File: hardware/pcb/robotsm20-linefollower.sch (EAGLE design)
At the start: 139 parts, among them Q5 BSS138LT3G, Q6 BSS138LT3G, Q7 BSS138LT3G, Q8 BSS138LT3G, U1 STM32F405RG

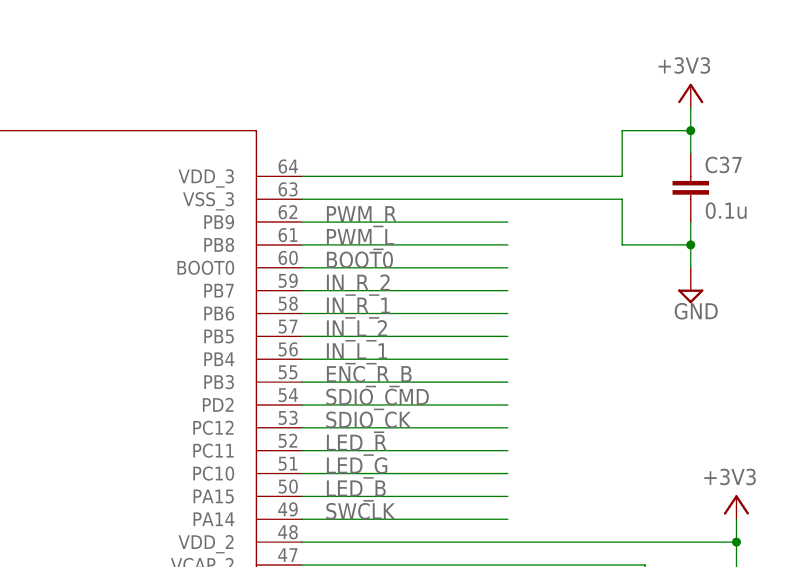
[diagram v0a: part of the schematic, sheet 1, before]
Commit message: Changed pinout on MCU for better layout to motor driver
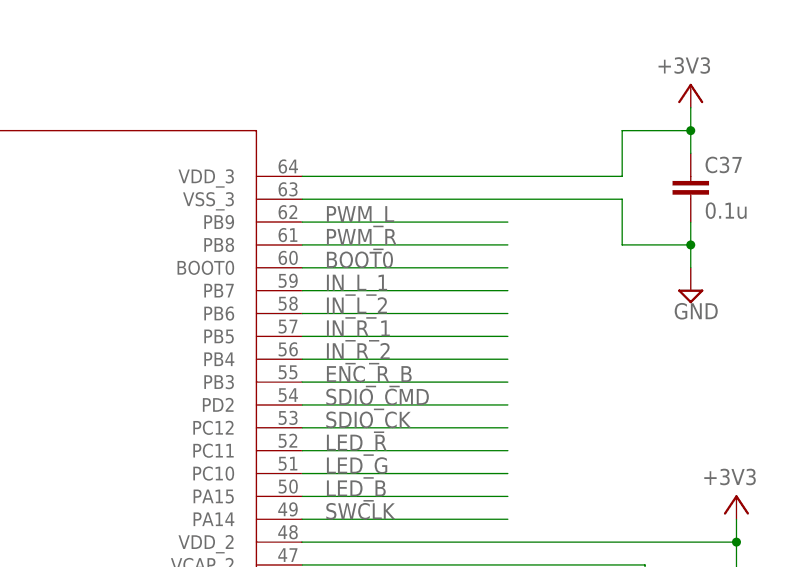
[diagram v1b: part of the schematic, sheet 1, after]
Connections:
- net IN_L_1: now also U1.PB7; no longer U1.PB4
- net IN_L_2: now also U1.PB6; no longer U1.PB5
- net IN_R_1: now also U1.PB5; no longer U1.PB6
- net IN_R_2: now also U1.PB4; no longer U1.PB7
- net PWM_L: now also U1.PB9; no longer U1.PB8
- net PWM_R: now also U1.PB8; no longer U1.PB9
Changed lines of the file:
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@@
 <?xml version="1.0" encoding="utf-8"?>
 <!DOCTYPE eagle SYSTEM "eagle.dtd">
-<eagle version="9.5.2">
+<eagle version="9.6.0">
 <drawing>
 <settings>
@@
 <net name="PWM_L" class="0">
 <segment>
-<wire x1="2.54" y1="15.24" x2="-20.32" y2="15.24" width="0.1524" layer="91"/>
-<pinref part="U1" gate="STM32F405RG" pin="PB8"/>
-<label x="-17.78" y="15.24" size="1.778" layer="95"/>
-</segment>
-</net>
-<net name="PWM_R" class="0">
-<segment>
-<wire x1="2.54" y1="17.78" x2="-20.32" y2="17.78" width="0.1524" layer="91"/>
 <pinref part="U1" gate="STM32F405RG" pin="PB9"/>
+<wire x1="-20.32" y1="17.78" x2="2.54" y2="17.78" width="0.1524" layer="91"/>
 <label x="-17.78" y="17.78" size="1.778" layer="95"/>
-</segment>
-</net>
-<net name="IN_R_2" class="0">
-<segment>
-<wire x1="2.54" y1="10.16" x2="-20.32" y2="10.16" width="0.1524" layer="91"/>
-<pinref part="U1" gate="STM32F405RG" pin="PB7"/>
-<label x="-17.78" y="10.16" size="1.778" layer="95"/>
 </segment>
 </net>
@@
 </segment>
 </net>
-<net name="IN_L_2" class="0">
-<segment>
-<wire x1="2.54" y1="5.08" x2="-20.32" y2="5.08" width="0.1524" layer="91"/>
-<pinref part="U1" gate="STM32F405RG" pin="PB5"/>
-<label x="-17.78" y="5.08" size="1.778" layer="95"/>
-</segment>
-</net>
-<net name="IN_R_1" class="0">
-<segment>
-<wire x1="2.54" y1="7.62" x2="-20.32" y2="7.62" width="0.1524" layer="91"/>
-<pinref part="U1" gate="STM32F405RG" pin="PB6"/>
-<label x="-17.78" y="7.62" size="1.778" layer="95"/>
-</segment>
-</net>
 <net name="ENC_R_B" class="0">
 <segment>
@@
 <pinref part="U1" gate="STM32F405RG" pin="PB3"/>
 <label x="-17.78" y="0" size="1.778" layer="95"/>
-</segment>
-</net>
-<net name="IN_L_1" class="0">
-<segment>
-<wire x1="2.54" y1="2.54" x2="-20.32" y2="2.54" width="0.1524" layer="91"/>
-<pinref part="U1" gate="STM32F405RG" pin="PB4"/>
-<label x="-17.78" y="2.54" size="1.778" layer="95"/>
 </segment>
 </net>
@@
 </segment>
 </net>
+<net name="PWM_R" class="0">
+<segment>
+<pinref part="U1" gate="STM32F405RG" pin="PB8"/>
+<wire x1="-20.32" y1="15.24" x2="2.54" y2="15.24" width="0.1524" layer="91"/>
+<label x="-17.78" y="15.24" size="1.778" layer="95"/>
+</segment>
+</net>
+<net name="IN_R_2" class="0">
+<segment>
+<pinref part="U1" gate="STM32F405RG" pin="PB4"/>
+<wire x1="-20.32" y1="2.54" x2="2.54" y2="2.54" width="0.1524" layer="91"/>
+<label x="-17.78" y="2.54" size="1.778" layer="95"/>
+</segment>
+</net>
+<net name="IN_R_1" class="0">
+<segment>
+<pinref part="U1" gate="STM32F405RG" pin="PB5"/>
+<wire x1="-20.32" y1="5.08" x2="2.54" y2="5.08" width="0.1524" layer="91"/>
+<label x="-17.78" y="5.08" size="1.778" layer="95"/>
+</segment>
+</net>
+<net name="IN_L_2" class="0">
+<segment>
+<pinref part="U1" gate="STM32F405RG" pin="PB6"/>
+<wire x1="-20.32" y1="7.62" x2="2.54" y2="7.62" width="0.1524" layer="91"/>
+<label x="-17.78" y="7.62" size="1.778" layer="95"/>
+</segment>
+</net>
+<net name="IN_L_1" class="0">
+<segment>
+<pinref part="U1" gate="STM32F405RG" pin="PB7"/>
+<wire x1="-20.32" y1="10.16" x2="2.54" y2="10.16" width="0.1524" layer="91"/>
+<label x="-17.78" y="10.16" size="1.778" layer="95"/>
+</segment>
+</net>

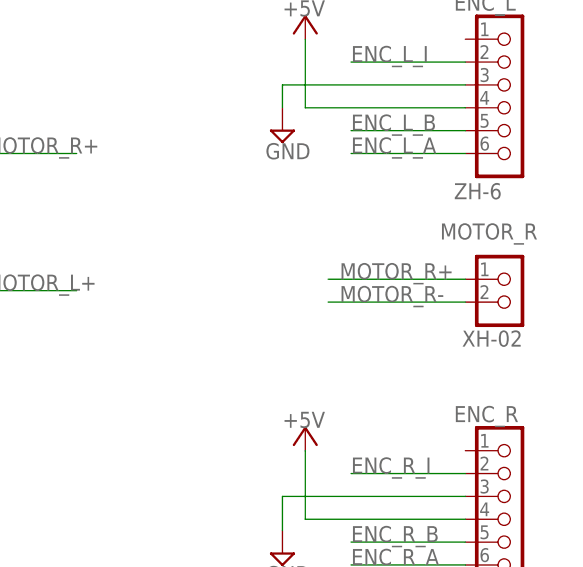
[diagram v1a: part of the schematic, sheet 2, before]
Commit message: Connect current amplifier and switch pins for Rmotor
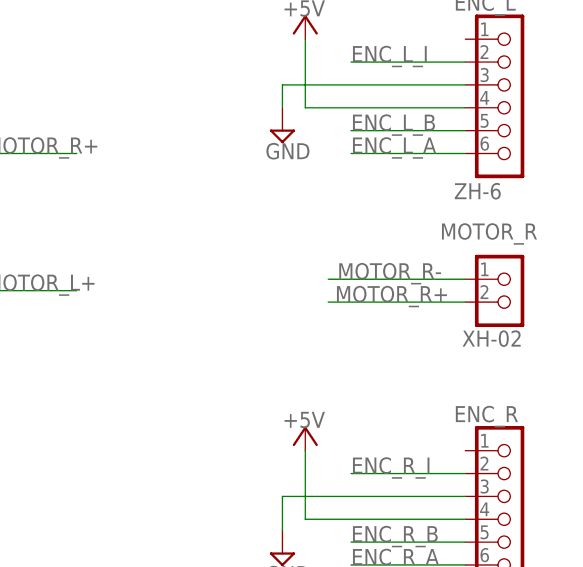
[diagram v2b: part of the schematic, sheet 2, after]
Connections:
- net MOTOR_R+: now also MOTOR_R.2; no longer MOTOR_R.1
- net MOTOR_R-: now also MOTOR_R.1; no longer MOTOR_R.2
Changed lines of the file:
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@@
 </segment>
 <segment>
-<pinref part="MOTOR_R" gate="G$1" pin="2"/>
-<wire x1="58.42" y1="29.21" x2="43.18" y2="29.21" width="0.1524" layer="91" grouprefs="MOTOR-CONNECTOR"/>
-<label x="44.45" y="29.21" size="1.778" layer="95"/>
+<pinref part="MOTOR_R" gate="G$1" pin="1"/>
+<wire x1="58.42" y1="31.75" x2="43.18" y2="31.75" width="0.1524" layer="91" grouprefs="MOTOR-CONNECTOR"/>
+<label x="44.196" y="31.75" size="1.778" layer="95" grouprefs="MOTOR-CONNECTOR"/>
 </segment>
 </net>
@@
 </segment>
 <segment>
-<pinref part="MOTOR_R" gate="G$1" pin="1"/>
-<wire x1="58.42" y1="31.75" x2="43.18" y2="31.75" width="0.1524" layer="91" grouprefs="MOTOR-CONNECTOR"/>
-<label x="44.45" y="31.75" size="1.778" layer="95"/>
+<pinref part="MOTOR_R" gate="G$1" pin="2"/>
+<wire x1="58.42" y1="29.21" x2="43.18" y2="29.21" width="0.1524" layer="91" grouprefs="MOTOR-CONNECTOR"/>
+<label x="43.942" y="29.21" size="1.778" layer="95" grouprefs="MOTOR-CONNECTOR"/>
 </segment>
 </net>

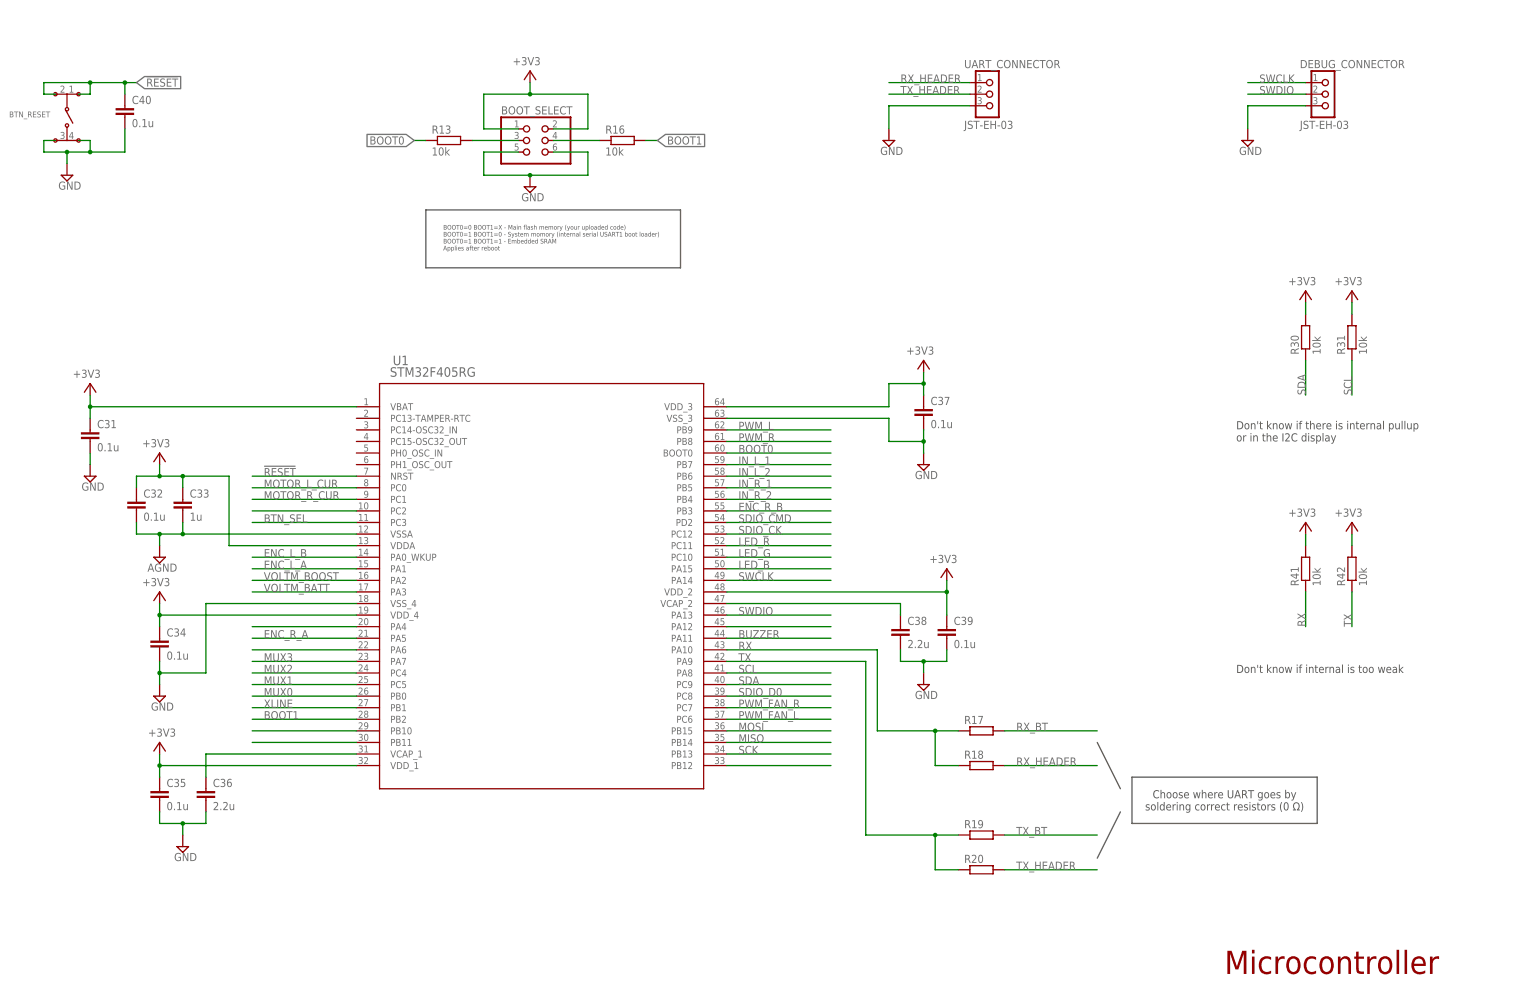
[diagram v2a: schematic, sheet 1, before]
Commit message: Changed to DGND for all MCU components
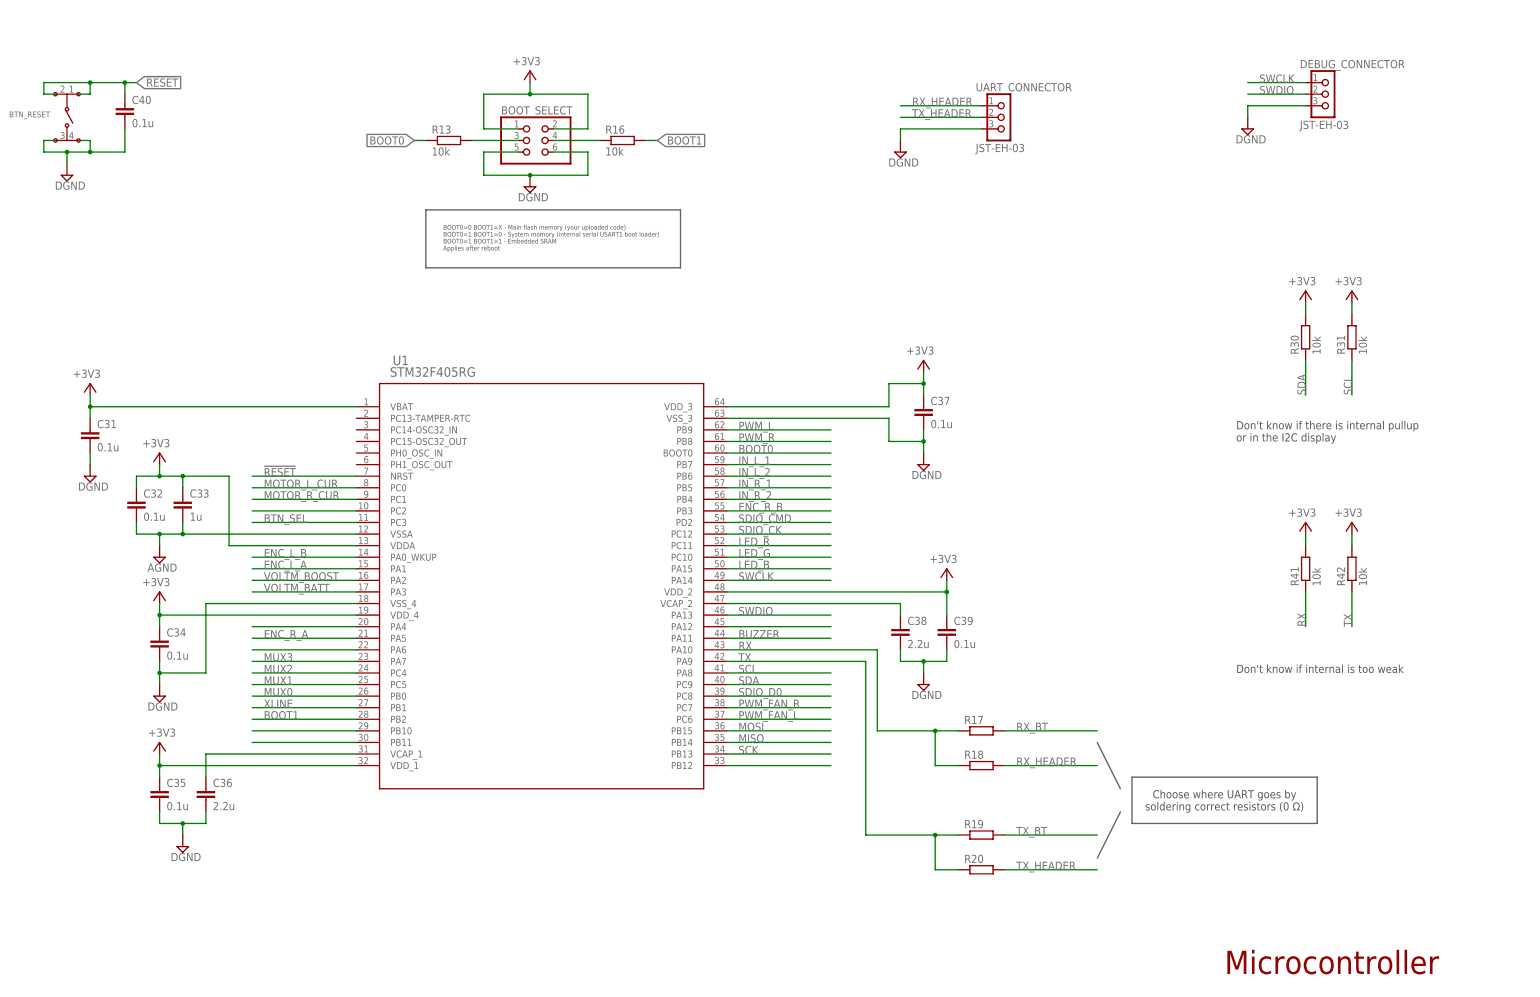
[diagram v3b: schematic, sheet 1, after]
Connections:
- new net DGND: BOOT_SELECT.5, BOOT_SELECT.6, BTN_RESET.3, BTN_RESET.4, BTN_SEL.3, BTN_SEL.4, BT_HC05.GND, BUCK.GND, BUCK.PAD, C10.2, C11.2, C12.2, C17.2, C31.2, C34.2, C35.2, C36.2, C37.2, C38.2, C39.2, C40.2, C46.2, C8.2, C9.2, DEBUG_CONNECTOR.3, ENC_L.3, ENC_R.3, LDO_3V3.GND, OLED_DISPLAY.GND, Q5.S, Q6.S, Q7.S, Q8.S, R47.2, R48.1, R6.1, R7.1, R8.1, SD_CARDHOLDER.VSS, U1.VSS_3, U1.VSS_4, UART_CONNECTOR.3
- net AGND: now also R44.2, XLINE.1
- net GND: no longer BOOT_SELECT.5, BOOT_SELECT.6, BTN_RESET.3, BTN_RESET.4, BTN_SEL.3, BTN_SEL.4, BT_HC05.GND, BUCK.GND, BUCK.PAD, C10.2, C11.2, C12.2, C17.2, C31.2, C34.2, C35.2, C36.2, C37.2, C38.2, C39.2, C40.2, C46.2, C8.2, C9.2, DEBUG_CONNECTOR.3, ENC_L.3, ENC_R.3, LDO_3V3.GND, OLED_DISPLAY.GND, Q5.S, Q6.S, Q7.S, Q8.S, R44.2, R47.2, R48.1, R6.1, R7.1, R8.1, SD_CARDHOLDER.VSS, U1.VSS_3, U1.VSS_4, UART_CONNECTOR.3, XLINE.1
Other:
- moved on the sheet: UART_CONNECTOR

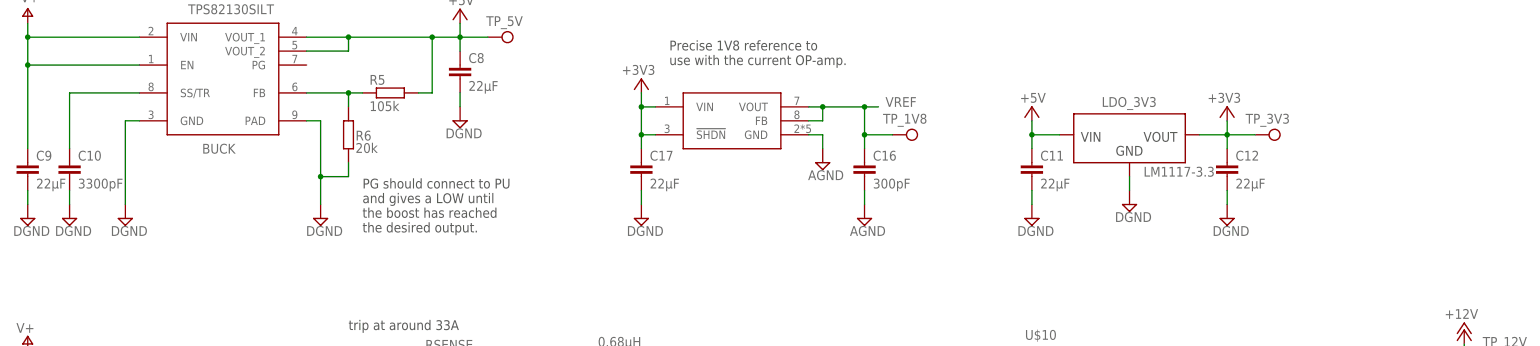
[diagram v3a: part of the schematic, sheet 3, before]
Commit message: Routed to motor driver
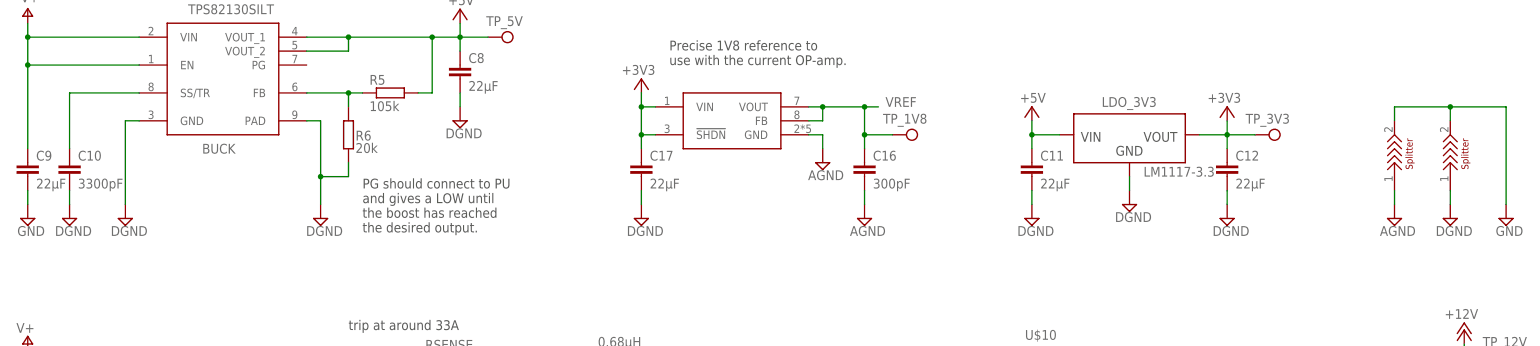
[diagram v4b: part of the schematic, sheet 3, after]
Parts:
- added U$4, U$6: SPLITTER, Isaks Bibliotek:SPLITTER
- C11, C12, C16, C17, C8: device rcl:C-EUC0805 -> rcl:C-EUC0603
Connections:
- net AGND: now also U$6.1
- net DGND: now also U$4.1; no longer C9.2
- net GND: now also C9.2, U$4.2, U$6.2

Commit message: Routed UART and I2C
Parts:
- C46, C47: device rcl:C-EUC0805 -> rcl:C-EUC0603
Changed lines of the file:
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@@
 <part name="R31" library="rcl" library_urn="urn:adsk.eagle:library:334" deviceset="R-EU_" device="R0603" package3d_urn="urn:adsk.eagle:package:23555/3" value="10k"/>
 <part name="BTN_SEL" library="CASE-Switches" library_urn="urn:adsk.eagle:library:7770839" deviceset="TSM2JSMA" device="" package3d_urn="urn:adsk.eagle:package:17798453/3"/>
-<part name="C46" library="rcl" library_urn="urn:adsk.eagle:library:334" deviceset="C-EU" device="C0805" package3d_urn="urn:adsk.eagle:package:23617/2" value="0.1u"/>
+<part name="C46" library="rcl" library_urn="urn:adsk.eagle:library:334" deviceset="C-EU" device="C0603" package3d_urn="urn:adsk.eagle:package:23616/2" value="0.1u"/>
 <part name="+3V6" library="supply1" library_urn="urn:adsk.eagle:library:371" deviceset="+3V3" device=""/>
 <part name="ENC_L" library="CASE-JST" library_urn="urn:adsk.eagle:library:5637561" deviceset="ZR_B6B-ZR" device="" package3d_urn="urn:adsk.eagle:package:5644773/2" value="ZH-6"/>
@@
 <part name="R47" library="rcl" library_urn="urn:adsk.eagle:library:334" deviceset="R-EU_" device="R0603" package3d_urn="urn:adsk.eagle:package:23555/3" value="10k"/>
 <part name="U$5" library="Isaks Bibliotek" library_urn="urn:adsk.eagle:library:11889733" deviceset="DIODE_1N4148WX" device="" package3d_urn="urn:adsk.eagle:package:12971321/3"/>
-<part name="C47" library="rcl" library_urn="urn:adsk.eagle:library:334" deviceset="C-EU" device="C0805" package3d_urn="urn:adsk.eagle:package:23617/2"/>
+<part name="C47" library="rcl" library_urn="urn:adsk.eagle:library:334" deviceset="C-EU" device="C0603" package3d_urn="urn:adsk.eagle:package:23616/2"/>
 <part name="XLINE" library="CASE-JST" library_urn="urn:adsk.eagle:library:5637561" deviceset="ZR_B7B-ZR" device="" package3d_urn="urn:adsk.eagle:package:5644772/2" value="ZH"/>
 <part name="+3V13" library="supply1" library_urn="urn:adsk.eagle:library:371" deviceset="+3V3" device=""/>
